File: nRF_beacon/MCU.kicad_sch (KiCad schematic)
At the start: 21 parts, among them U1 nRF54L15-QFAA, X1 32MHz

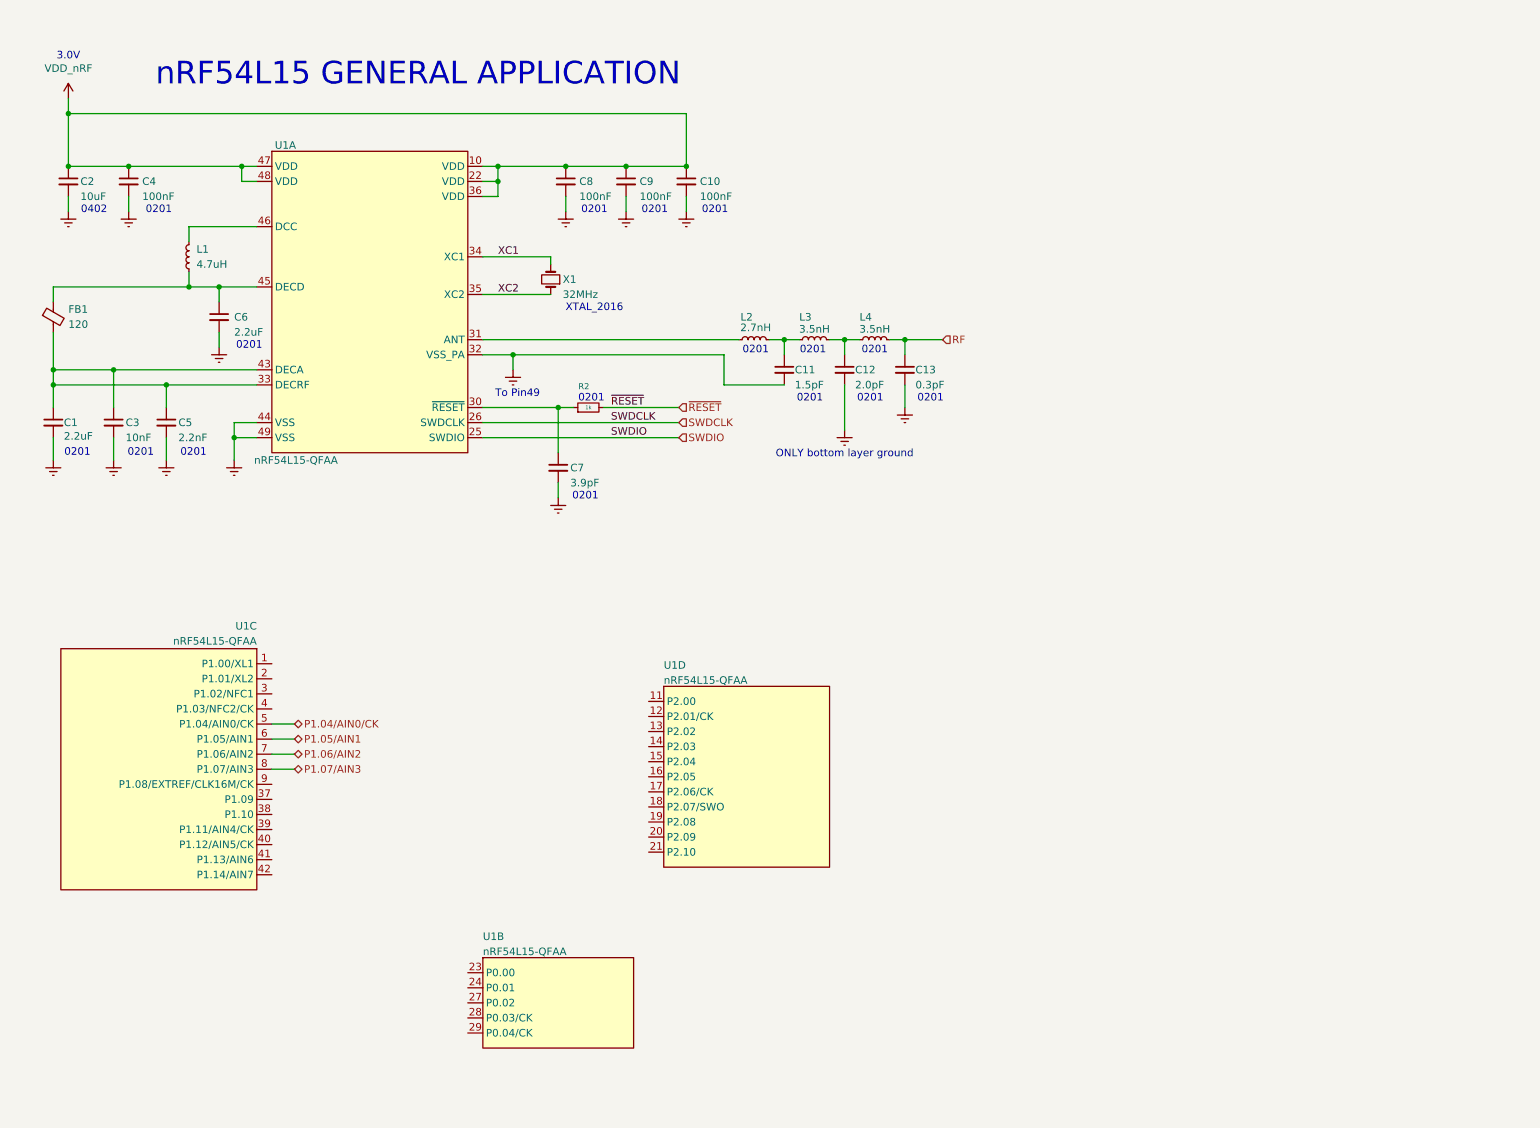
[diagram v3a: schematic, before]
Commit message: Updated nPM schematic. Added TWI and debug connector
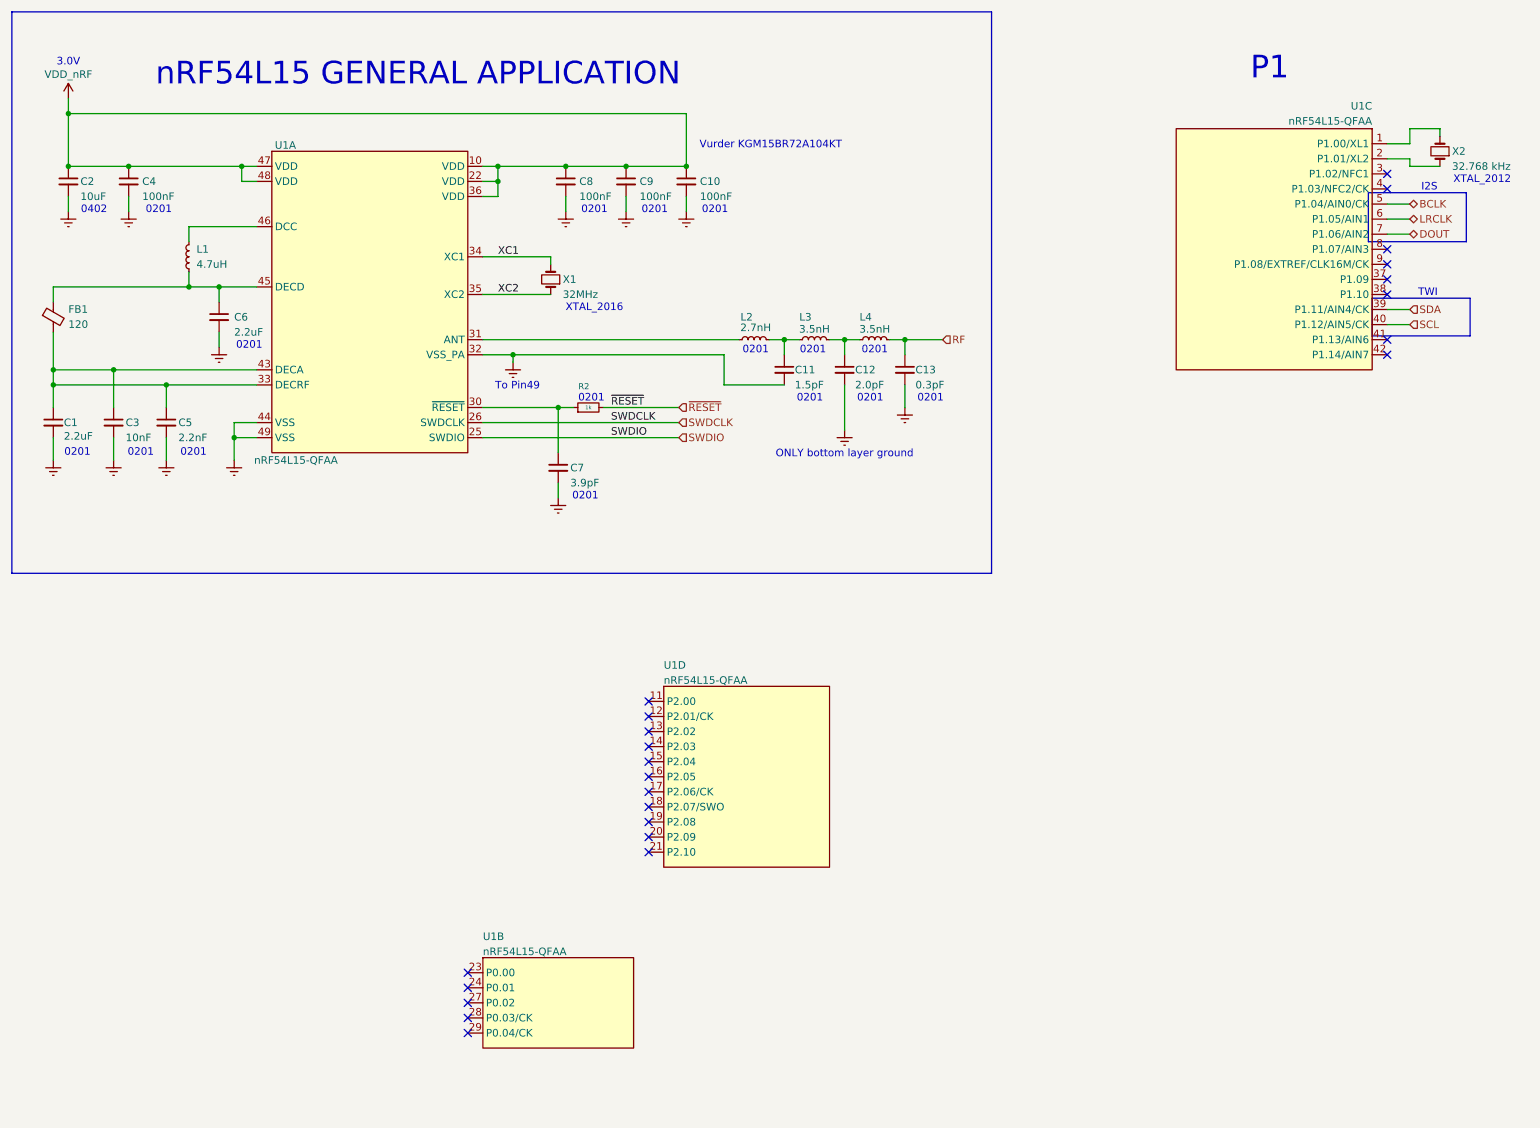
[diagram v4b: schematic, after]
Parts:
- added X2: 32.768 kHz, Crystal:Crystal_SMD_2012-2Pin_2.0x1.2mm_HandSoldering, symbol Device:Crystal_Small
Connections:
- net at U1.1 (P1.00/XL1): now also X2.2
- net at U1.2 (P1.01/XL2): now also X2.1
- net SDA: now reaches U1.39 (P1.11/AIN4/CK)
- net SCL: now reaches U1.40 (P1.12/AIN5/CK)
- net P1.04/AIN0/CK renamed BCLK
- net P1.05/AIN1 renamed LRCLK
- net P1.06/AIN2 renamed DOUT
- net P1.07/AIN3: no longer names the net of U1.8 (P1.07/AIN3)
- no-connect marks 0 -> 24
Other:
- note added: "I2S"
- note added: "P1"
- note added: "TWI"
- note added: "Vurder KGM15BR72A104KT"
- note added: "XTAL_2012"
- moved on the sheet: U1C

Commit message: Added LEDs and BUCK supply from VSYS
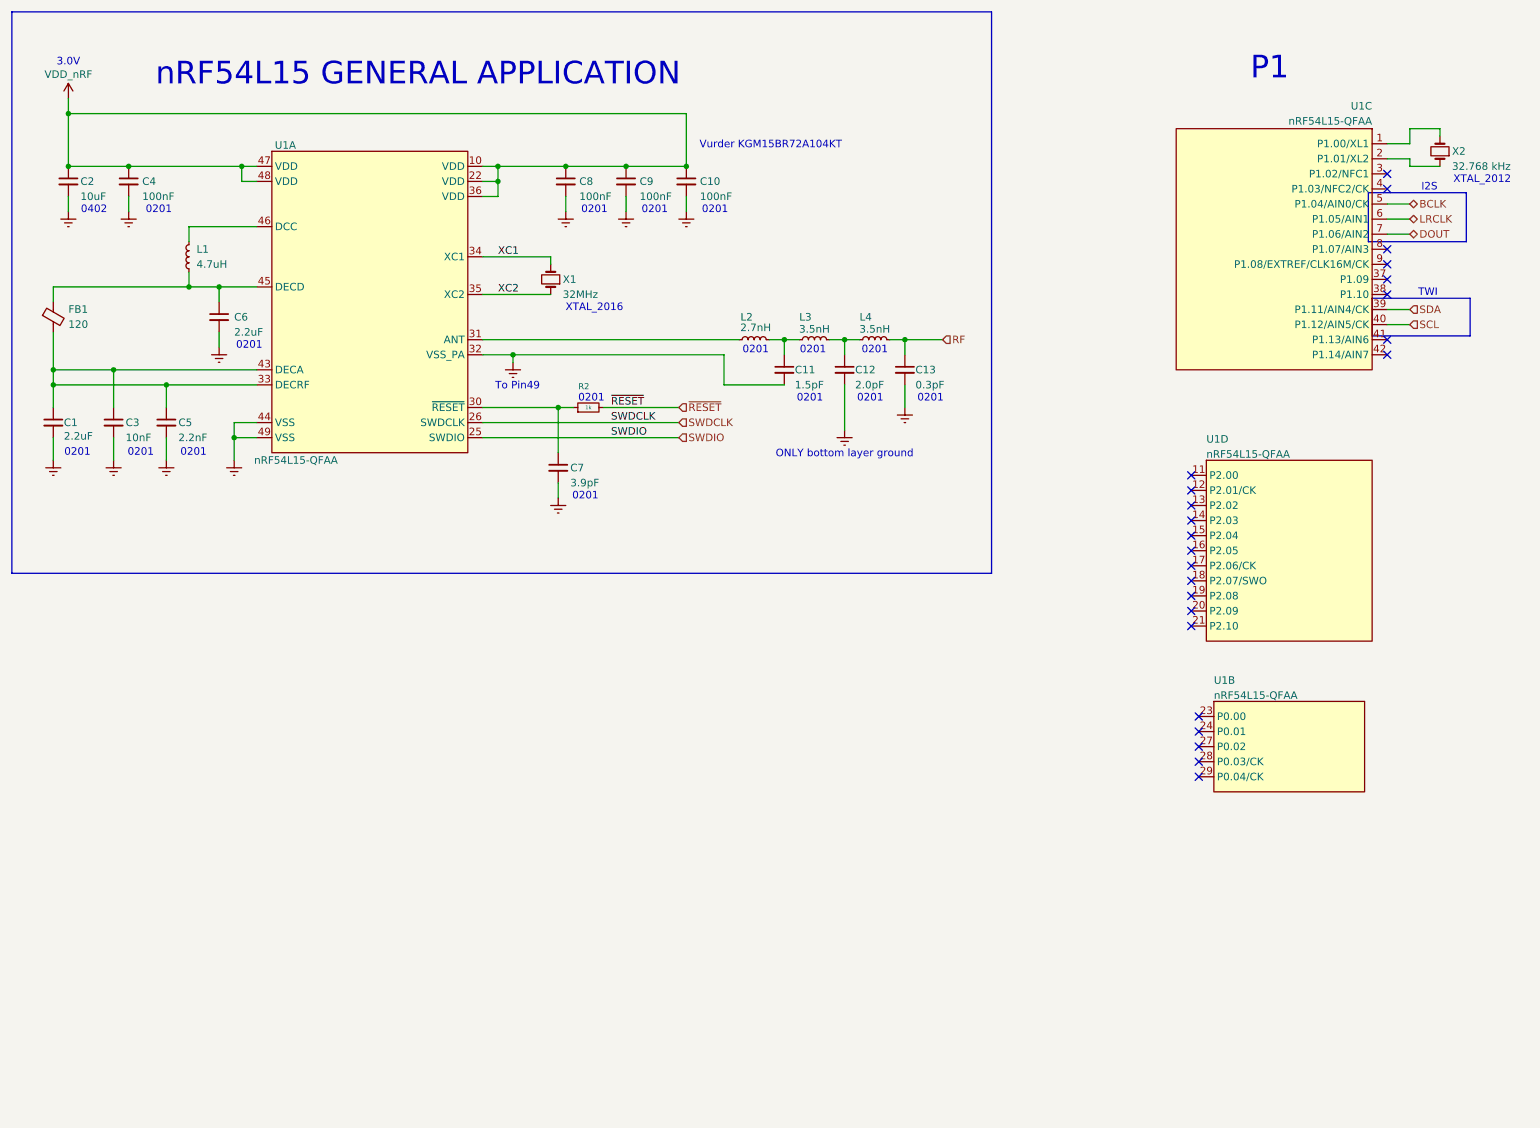
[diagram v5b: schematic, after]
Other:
- moved on the sheet: U1B, U1D
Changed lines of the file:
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@@
 	)
 	(no_connect
-		(at 119.38 143.51)
+		(at 210.82 105.41)
 	)
 	(no_connect
-		(at 88.9 173.99)
+		(at 212.09 130.81)
 	)
 	(no_connect
-		(at 119.38 151.13)
+		(at 210.82 113.03)
 	)
 	(no_connect
@@
 	)
 	(no_connect
-		(at 119.38 148.59)
+		(at 210.82 110.49)
 	)
 	(no_connect
-		(at 119.38 146.05)
+		(at 210.82 107.95)
 	)
 	(no_connect
@@
 	)
 	(no_connect
-		(at 119.38 140.97)
+		(at 210.82 102.87)
 	)
 	(no_connect
-		(at 119.38 153.67)
+		(at 210.82 115.57)
 	)
 	(no_connect
-		(at 119.38 133.35)
+		(at 210.82 95.25)
 	)
 	(no_connect
-		(at 119.38 130.81)
+		(at 210.82 92.71)
 	)
 	(no_connect
@@
 	)
 	(no_connect
-		(at 88.9 181.61)
+		(at 212.09 138.43)
 	)
 	(no_connect
-		(at 119.38 128.27)
+		(at 210.82 90.17)
 	)
 	(no_connect
@@
 	)
 	(no_connect
-		(at 88.9 176.53)
+		(at 212.09 133.35)
 	)
 	(no_connect
-		(at 88.9 179.07)
+		(at 212.09 135.89)
 	)
 	(no_connect
@@
 	)
 	(no_connect
-		(at 119.38 138.43)
+		(at 210.82 100.33)
 	)
 	(no_connect
-		(at 88.9 184.15)
+		(at 212.09 140.97)
 	)
 	(no_connect
-		(at 119.38 135.89)
+		(at 210.82 97.79)
 	)
 	(wire
@@
 	(symbol
 		(lib_id "Ekse:nRF54L15")
-		(at 121.92 156.21 0)
+		(at 213.36 118.11 0)
 		(unit 4)
 		(exclude_from_sim no)
@@
 		(dnp no)
 		(property "Reference" "U1"
-			(at 121.92 122.174 0)
+			(at 213.36 84.074 0)
 			(effects
 				(font
@@
 		)
 		(property "Value" "nRF54L15-QFAA"
-			(at 121.92 124.714 0)
+			(at 213.36 86.614 0)
 			(effects
 				(font
@@
 		)
 		(property "Footprint" "Ekse:QFN48_6X6_NOR"
-			(at 121.92 156.21 0)
+			(at 213.36 118.11 0)
 			(effects
 				(font
@@
 		)
 		(property "Datasheet" ""
-			(at 121.92 156.21 0)
+			(at 213.36 118.11 0)
 			(effects
 				(font
@@
 		)
 		(property "Description" ""
-			(at 121.92 156.21 0)
+			(at 213.36 118.11 0)
 			(effects
 				(font
@@
 		)
 		(property "MPN" "NRF54L15-QFAA-R7"
-			(at 121.92 156.21 0)
+			(at 213.36 118.11 0)
 			(effects
 				(font
@@
 		)
 		(property "Price" "23.08"
-			(at 121.92 156.21 0)
+			(at 213.36 118.11 0)
 			(effects
 				(font
@@
 	(symbol
 		(lib_id "Ekse:nRF54L15")
-		(at 91.44 186.69 0)
+		(at 214.63 143.51 0)
 		(unit 2)
 		(exclude_from_sim no)
@@
 		(dnp no)
 		(property "Reference" "U1"
-			(at 91.44 167.894 0)
+			(at 214.63 124.714 0)
 			(effects
 				(font
@@
 		)
 		(property "Value" "nRF54L15-QFAA"
-			(at 91.44 170.434 0)
+			(at 214.63 127.254 0)
 			(effects
 				(font
@@
 		)
 		(property "Footprint" "Ekse:QFN48_6X6_NOR"
-			(at 91.44 186.69 0)
+			(at 214.63 143.51 0)
 			(effects
 				(font
@@
 		)
 		(property "Datasheet" ""
-			(at 91.44 186.69 0)
+			(at 214.63 143.51 0)
 			(effects
 				(font
@@
 		)
 		(property "Description" ""
-			(at 91.44 186.69 0)
+			(at 214.63 143.51 0)
 			(effects
 				(font
@@
 		)
 		(property "MPN" "NRF54L15-QFAA-R7"
-			(at 91.44 186.69 0)
+			(at 214.63 143.51 0)
 			(effects
 				(font
@@
 		)
 		(property "Price" "23.08"
-			(at 91.44 186.69 0)
+			(at 214.63 143.51 0)
 			(effects
 				(font

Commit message: Finished first schematic draft. Ready for layout
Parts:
- FB1: MPN (none) -> MMZ0603Y121CT000; Price (none) -> 1.3
- R2: footprint (none) -> Resistor_SMD:R_0201_0603Metric_Pad0.64x0.40mm_HandSolder
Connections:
- net P1.09: now reaches U1.37 (P1.09)
- net P1.10: now reaches U1.38 (P1.10)
- net P1.13: now reaches U1.41 (P1.13/AIN6)
- net P1.14: now reaches U1.42 (P1.14/AIN7)
- net P1.07: now reaches U1.8 (P1.07/AIN3)
- net P1.08: now reaches U1.9 (P1.08/EXTREF/CLK16M/CK)
- no-connect marks 24 -> 18
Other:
- moved on the sheet: U1B, U1C, U1D, X2

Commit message: Began matching network layout
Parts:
- C1, C10, C11, C12, C13, C3, C4, C5, C6, C7, C8, C9: footprint Capacitor_SMD:C_0201_0603Metric_Pad0.64x0.40mm_HandSolder -> Capacitor_SMD:C_0201_0603Metric
- C2: footprint Capacitor_SMD:C_0402_1005Metric_Pad0.74x0.62mm_HandSolder -> Capacitor_SMD:C_0402_1005Metric
- FB1, L2, L3, L4: footprint Inductor_SMD:L_0201_0603Metric_Pad0.64x0.40mm_HandSolder -> Inductor_SMD:L_0201_0603Metric
- L1: footprint Inductor_SMD:L_0603_1608Metric_Pad1.05x0.95mm_HandSolder -> Inductor_SMD:L_0603_1608Metric
- R2: footprint Resistor_SMD:R_0201_0603Metric_Pad0.64x0.40mm_HandSolder -> Resistor_SMD:R_0201_0603Metric
- X2: footprint Crystal:Crystal_SMD_2012-2Pin_2.0x1.2mm_HandSoldering -> Crystal:Crystal_SMD_2012-2Pin_2.0x1.2mm
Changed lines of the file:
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@@
 			)
 		)
-		(property "Footprint" "Capacitor_SMD:C_0201_0603Metric_Pad0.64x0.40mm_HandSolder"
+		(property "Footprint" "Capacitor_SMD:C_0201_0603Metric"
 			(at 142.24 72.39 0)
 			(effects
@@
 			)
 		)
-		(property "Footprint" "Inductor_SMD:L_0603_1608Metric_Pad1.05x0.95mm_HandSolder"
+		(property "Footprint" "Inductor_SMD:L_0603_1608Metric"
 			(at 41.91 53.34 0)
 			(effects
@@
 			)
 		)
-		(property "Footprint" "Capacitor_SMD:C_0201_0603Metric_Pad0.64x0.40mm_HandSolder"
+		(property "Footprint" "Capacitor_SMD:C_0201_0603Metric"
 			(at 125.73 40.64 0)
 			(effects
@@
 			)
 		)
-		(property "Footprint" "Inductor_SMD:L_0201_0603Metric_Pad0.64x0.40mm_HandSolder"
+		(property "Footprint" "Inductor_SMD:L_0201_0603Metric"
 			(at 17.272 63.5 90)
 			(effects
@@
 			)
 		)
-		(property "Footprint" "Capacitor_SMD:C_0201_0603Metric_Pad0.64x0.40mm_HandSolder"
+		(property "Footprint" "Capacitor_SMD:C_0201_0603Metric"
 			(at 115.57 40.64 0)
 			(effects
@@
 			)
 		)
-		(property "Footprint" "Capacitor_SMD:C_0201_0603Metric_Pad0.64x0.40mm_HandSolder"
+		(property "Footprint" "Capacitor_SMD:C_0201_0603Metric"
 			(at 105.41 40.64 0)
 			(effects
@@
 			)
 		)
-		(property "Footprint" "Capacitor_SMD:C_0201_0603Metric_Pad0.64x0.40mm_HandSolder"
+		(property "Footprint" "Capacitor_SMD:C_0201_0603Metric"
 			(at 31.75 40.64 0)
 			(effects
@@
 			)
 		)
-		(property "Footprint" "Capacitor_SMD:C_0402_1005Metric_Pad0.74x0.62mm_HandSolder"
+		(property "Footprint" "Capacitor_SMD:C_0402_1005Metric"
 			(at 21.59 40.64 0)
 			(effects
@@
 			)
 		)
-		(property "Footprint" "Capacitor_SMD:C_0201_0603Metric_Pad0.64x0.40mm_HandSolder"
+		(property "Footprint" "Capacitor_SMD:C_0201_0603Metric"
 			(at 104.14 88.9 0)
 			(effects
@@
 			)
 		)
-		(property "Footprint" "Capacitor_SMD:C_0201_0603Metric_Pad0.64x0.40mm_HandSolder"
+		(property "Footprint" "Capacitor_SMD:C_0201_0603Metric"
 			(at 152.4 72.39 0)
 			(effects
@@
 			)
 		)
-		(property "Footprint" "Capacitor_SMD:C_0201_0603Metric_Pad0.64x0.40mm_HandSolder"
+		(property "Footprint" "Capacitor_SMD:C_0201_0603Metric"
 			(at 38.1 81.28 0)
 			(effects
@@
 			)
 		)
-		(property "Footprint" "Inductor_SMD:L_0201_0603Metric_Pad0.64x0.40mm_HandSolder"
+		(property "Footprint" "Inductor_SMD:L_0201_0603Metric"
 			(at 137.16 67.31 0)
 			(effects
@@
 			)
 		)
-		(property "Footprint" "Capacitor_SMD:C_0201_0603Metric_Pad0.64x0.40mm_HandSolder"
+		(property "Footprint" "Capacitor_SMD:C_0201_0603Metric"
 			(at 46.99 63.5 0)
 			(effects
@@
 			)
 		)
-		(property "Footprint" "Resistor_SMD:R_0201_0603Metric_Pad0.64x0.40mm_HandSolder"
+		(property "Footprint" "Resistor_SMD:R_0201_0603Metric"
 			(at 109.22 78.74 0)
 			(effects
@@
 			)
 		)
-		(property "Footprint" "Capacitor_SMD:C_0201_0603Metric_Pad0.64x0.40mm_HandSolder"
+		(property "Footprint" "Capacitor_SMD:C_0201_0603Metric"
 			(at 19.05 81.28 0)
 			(effects
@@
 			)
 		)
-		(property "Footprint" "Capacitor_SMD:C_0201_0603Metric_Pad0.64x0.40mm_HandSolder"
+		(property "Footprint" "Capacitor_SMD:C_0201_0603Metric"
 			(at 162.56 72.39 0)
 			(effects
@@
 			)
 		)
-		(property "Footprint" "Crystal:Crystal_SMD_2012-2Pin_2.0x1.2mm_HandSoldering"
+		(property "Footprint" "Crystal:Crystal_SMD_2012-2Pin_2.0x1.2mm"
 			(at 234.95 34.29 0)
 			(effects
@@
 			)
 		)
-		(property "Footprint" "Capacitor_SMD:C_0201_0603Metric_Pad0.64x0.40mm_HandSolder"
+		(property "Footprint" "Capacitor_SMD:C_0201_0603Metric"
 			(at 29.21 81.28 0)
 			(effects
@@
 			)
 		)
-		(property "Footprint" "Inductor_SMD:L_0201_0603Metric_Pad0.64x0.40mm_HandSolder"
+		(property "Footprint" "Inductor_SMD:L_0201_0603Metric"
 			(at 157.48 67.31 0)
 			(effects
@@
 			)
 		)
-		(property "Footprint" "Inductor_SMD:L_0201_0603Metric_Pad0.64x0.40mm_HandSolder"
+		(property "Footprint" "Inductor_SMD:L_0201_0603Metric"
 			(at 147.32 67.31 0)
 			(effects
